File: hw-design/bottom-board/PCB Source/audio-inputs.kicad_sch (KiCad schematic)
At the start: 88 parts, among them J7 NYS215, J8 NYS215, Q10 J110, Q11 J110, Q12 2N7002, Q13 2N7002, Q14 J110, Q15 J110, Q16 2N7002, Q9 2N7002, U22 LM833DR2G, U8 LM4562

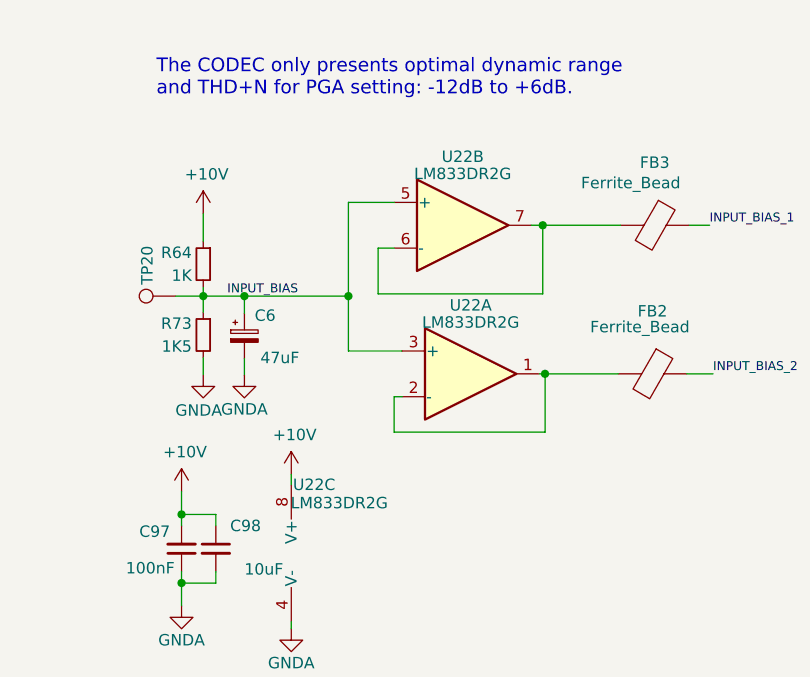
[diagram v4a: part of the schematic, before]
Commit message: mainboard: correct CC TX pin + update fabrication files
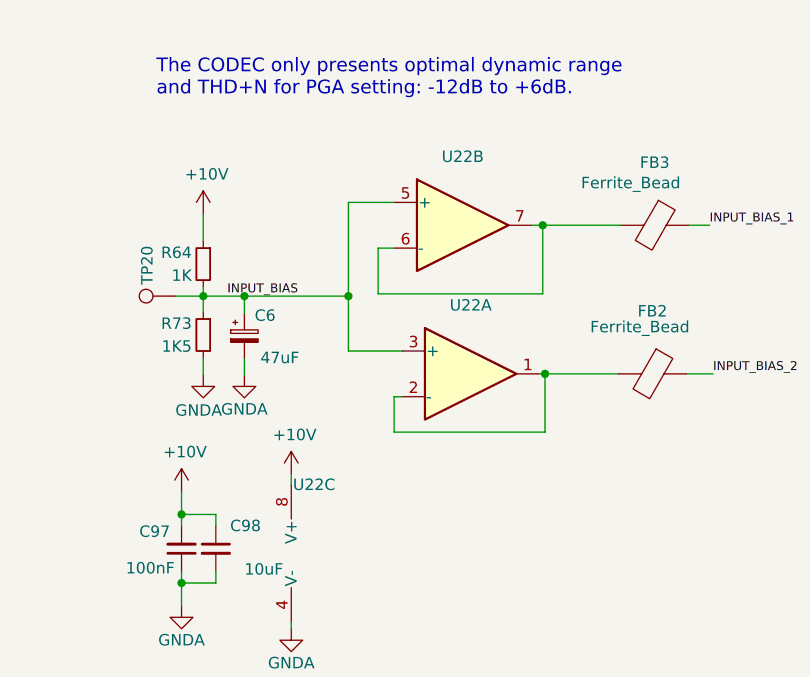
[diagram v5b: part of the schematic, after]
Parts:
- U22: value LM833DR2G -> (none); footprint Package_SO:SOIC-8_3.9x4.9mm_P1.27mm -> (none); MPN LM833DR2G -> OPA1678IDR; MPN2 OPA1678IDR -> LM833DR2G
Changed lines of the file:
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@@
     (pin "2")
     (pin "3")
+    (pin "5")
+    (pin "6")
+    (pin "7")
+    (pin "4")
+    (pin "8")
   )
   (symbol (lib_id "bottom-board-rescue:LM4562-Amplifier_Operational") (at 111.633 37.211 0) (unit 2)
@@
       (effects (font (size 1.27 1.27)) hide)
     )
+    (pin "1")
+    (pin "2")
+    (pin "3")
     (pin "5")
     (pin "6")
     (pin "7")
+    (pin "4")
+    (pin "8")
   )
   (symbol (lib_id "bottom-board-rescue:LM4562-Amplifier_Operational") (at 255.27 144.399 0) (unit 3)
@@
       (effects (font (size 1.27 1.27)) hide)
     )
+    (pin "1")
+    (pin "2")
+    (pin "3")
+    (pin "5")
+    (pin "6")
+    (pin "7")
     (pin "4")
     (pin "8")
@@
     (in_bom yes) (on_board yes)
     (property "Reference" "U22" (id 0) (at 240.919 69.723 0))
-    (property "Value" "LM833DR2G" (id 1) (at 240.919 71.628 0))
-    (property "Footprint" "Package_SO:SOIC-8_3.9x4.9mm_P1.27mm" (id 2) (at 240.919 77.343 0)
+    (property "Value" "" (id 1) (at 240.919 71.628 0))
+    (property "Footprint" "" (id 2) (at 240.919 77.343 0)
       (effects (font (size 1.27 1.27)) hide)
     )
@@
       (effects (font (size 1.27 1.27)) hide)
     )
-    (property "MPN" "LM833DR2G" (id 4) (at 158.369 119.253 0)
-      (effects (font (size 1.27 1.27)) hide)
-    )
-    (property "MPN2" "OPA1678IDR" (id 5) (at 240.919 77.343 0)
-      (effects (font (size 1.524 1.524)) hide)
-    )
+    (property "MPN" "OPA1678IDR" (id 4) (at 158.369 119.253 0)
+      (effects (font (size 1.27 1.27)) hide)
+    )
+    (property "MPN2" "LM833DR2G" (id 5) (at 240.919 77.343 0)
+      (effects (font (size 1.524 1.524)) hide)
+    )
+    (pin "1")
+    (pin "2")
+    (pin "3")
     (pin "5")
     (pin "6")
     (pin "7")
+    (pin "4")
+    (pin "8")
   )
   (symbol (lib_id "bottom-board-rescue:LM4562-Amplifier_Operational") (at 224.409 113.792 0) (unit 3)
     (in_bom yes) (on_board yes)
     (property "Reference" "U22" (id 0) (at 224.409 106.172 0))
-    (property "Value" "LM833DR2G" (id 1) (at 227.203 108.204 0))
-    (property "Footprint" "Package_SO:SOIC-8_3.9x4.9mm_P1.27mm" (id 2) (at 224.409 113.792 0)
+    (property "Value" "" (id 1) (at 227.203 108.204 0))
+    (property "Footprint" "" (id 2) (at 224.409 113.792 0)
       (effects (font (size 1.27 1.27)) hide)
     )
@@
       (effects (font (size 1.27 1.27)) hide)
     )
-    (property "MPN" "LM833DR2G" (id 4) (at 141.859 155.702 0)
-      (effects (font (size 1.27 1.27)) hide)
-    )
-    (property "MPN2" "OPA1678IDR" (id 5) (at 224.409 113.792 0)
-      (effects (font (size 1.524 1.524)) hide)
-    )
+    (property "MPN" "OPA1678IDR" (id 4) (at 141.859 155.702 0)
+      (effects (font (size 1.27 1.27)) hide)
+    )
+    (property "MPN2" "LM833DR2G" (id 5) (at 224.409 113.792 0)
+      (effects (font (size 1.524 1.524)) hide)
+    )
+    (pin "1")
+    (pin "2")
+    (pin "3")
+    (pin "5")
+    (pin "6")
+    (pin "7")
     (pin "4")
     (pin "8")
@@
     (in_bom yes) (on_board yes)
     (property "Reference" "U22" (id 0) (at 241.808 86.233 0))
-    (property "Value" "LM833DR2G" (id 1) (at 241.808 88.138 0))
-    (property "Footprint" "Package_SO:SOIC-8_3.9x4.9mm_P1.27mm" (id 2) (at 241.808 93.853 0)
+    (property "Value" "" (id 1) (at 241.808 88.138 0))
+    (property "Footprint" "" (id 2) (at 241.808 93.853 0)
       (effects (font (size 1.27 1.27)) hide)
     )
@@
       (effects (font (size 1.27 1.27)) hide)
     )
-    (property "MPN" "LM833DR2G" (id 4) (at 159.258 135.763 0)
-      (effects (font (size 1.27 1.27)) hide)
-    )
-    (property "MPN2" "OPA1678IDR" (id 5) (at 241.808 93.853 0)
+    (property "MPN" "OPA1678IDR" (id 4) (at 159.258 135.763 0)
+      (effects (font (size 1.27 1.27)) hide)
+    )
+    (property "MPN2" "LM833DR2G" (id 5) (at 241.808 93.853 0)
       (effects (font (size 1.524 1.524)) hide)
     )
@@
     (pin "2")
     (pin "3")
+    (pin "5")
+    (pin "6")
+    (pin "7")
+    (pin "4")
+    (pin "8")
   )
   (symbol (lib_id "power:+10V") (at 221.869 105.029 0) (unit 1)
